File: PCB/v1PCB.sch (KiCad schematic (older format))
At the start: 223 parts, among them SW1 SW_PUSH, SW2 SW_PUSH, U1 STM32F072CBUx, U2 MCP1700-3302E_SOT23

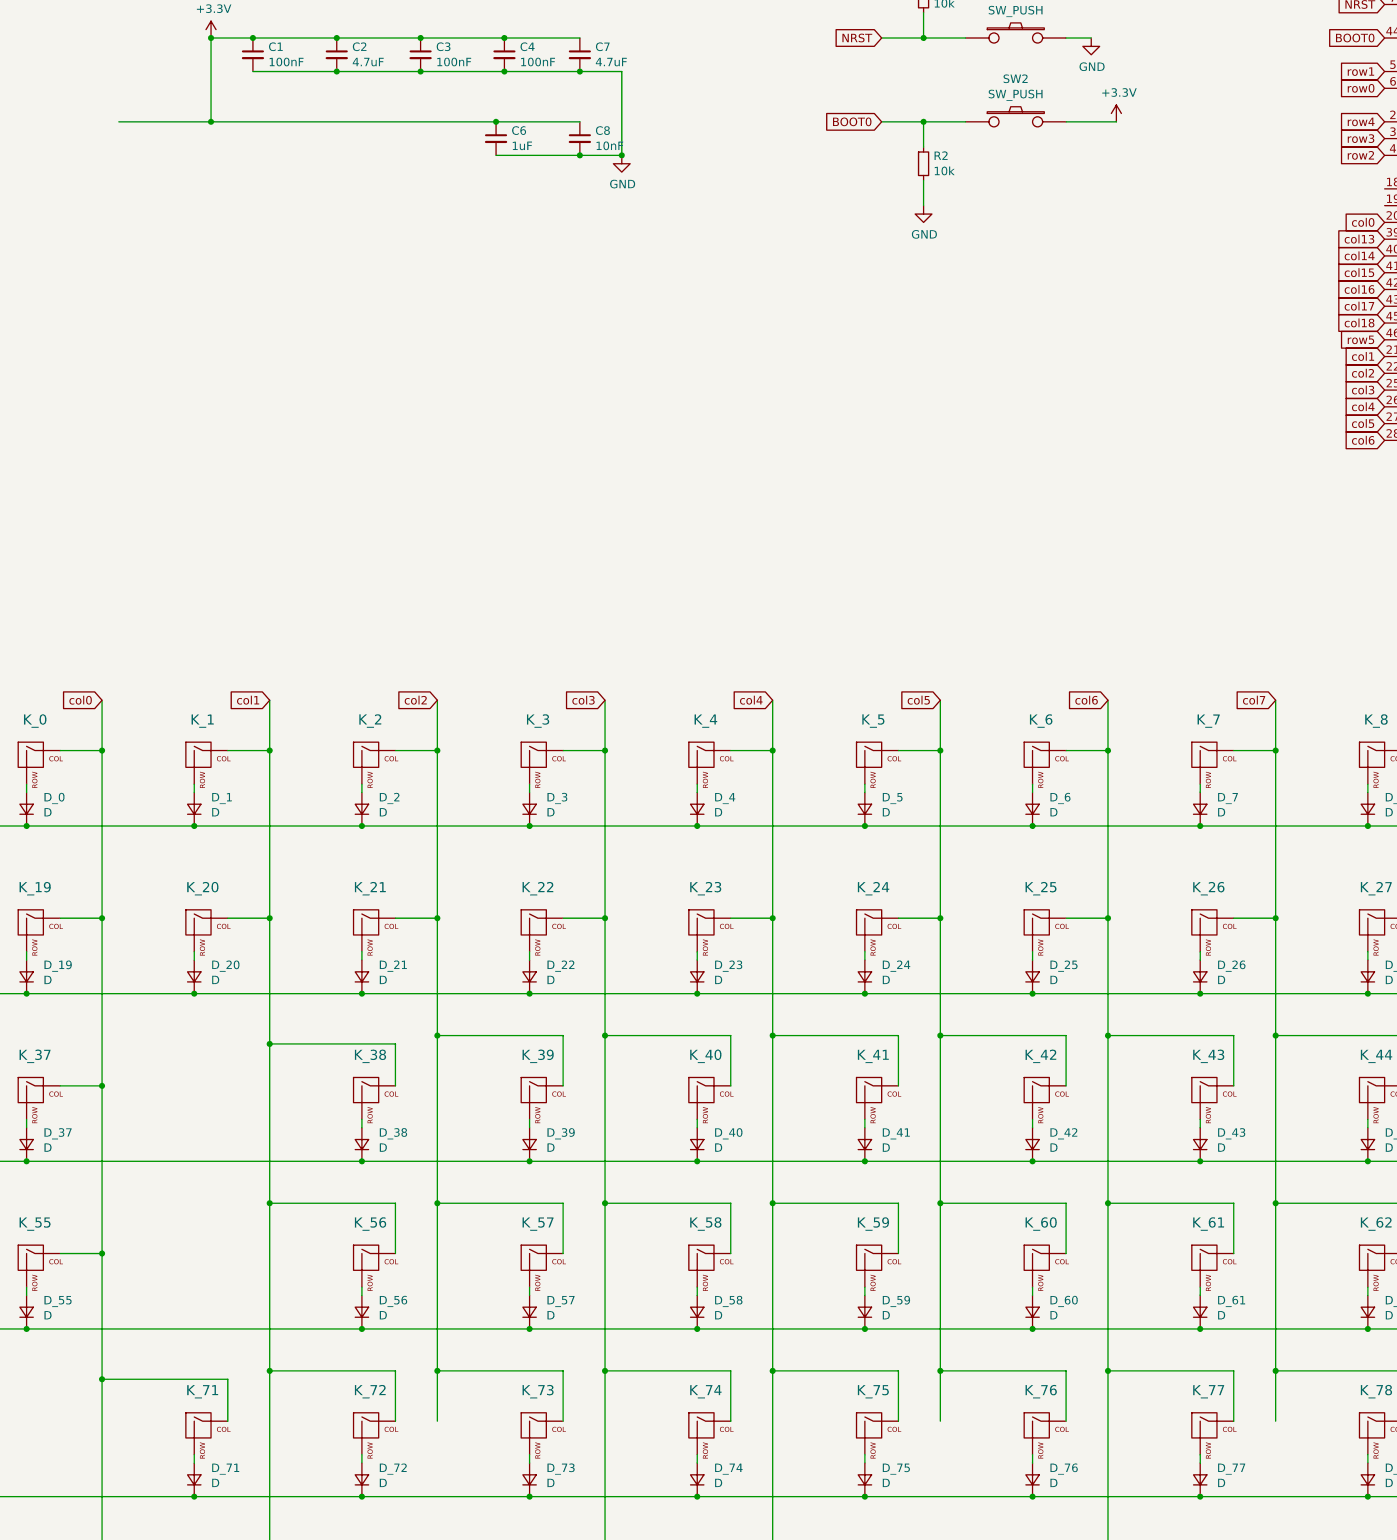
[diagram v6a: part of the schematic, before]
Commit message: PCB is being produced, because fuck it. CAD is being quoted.
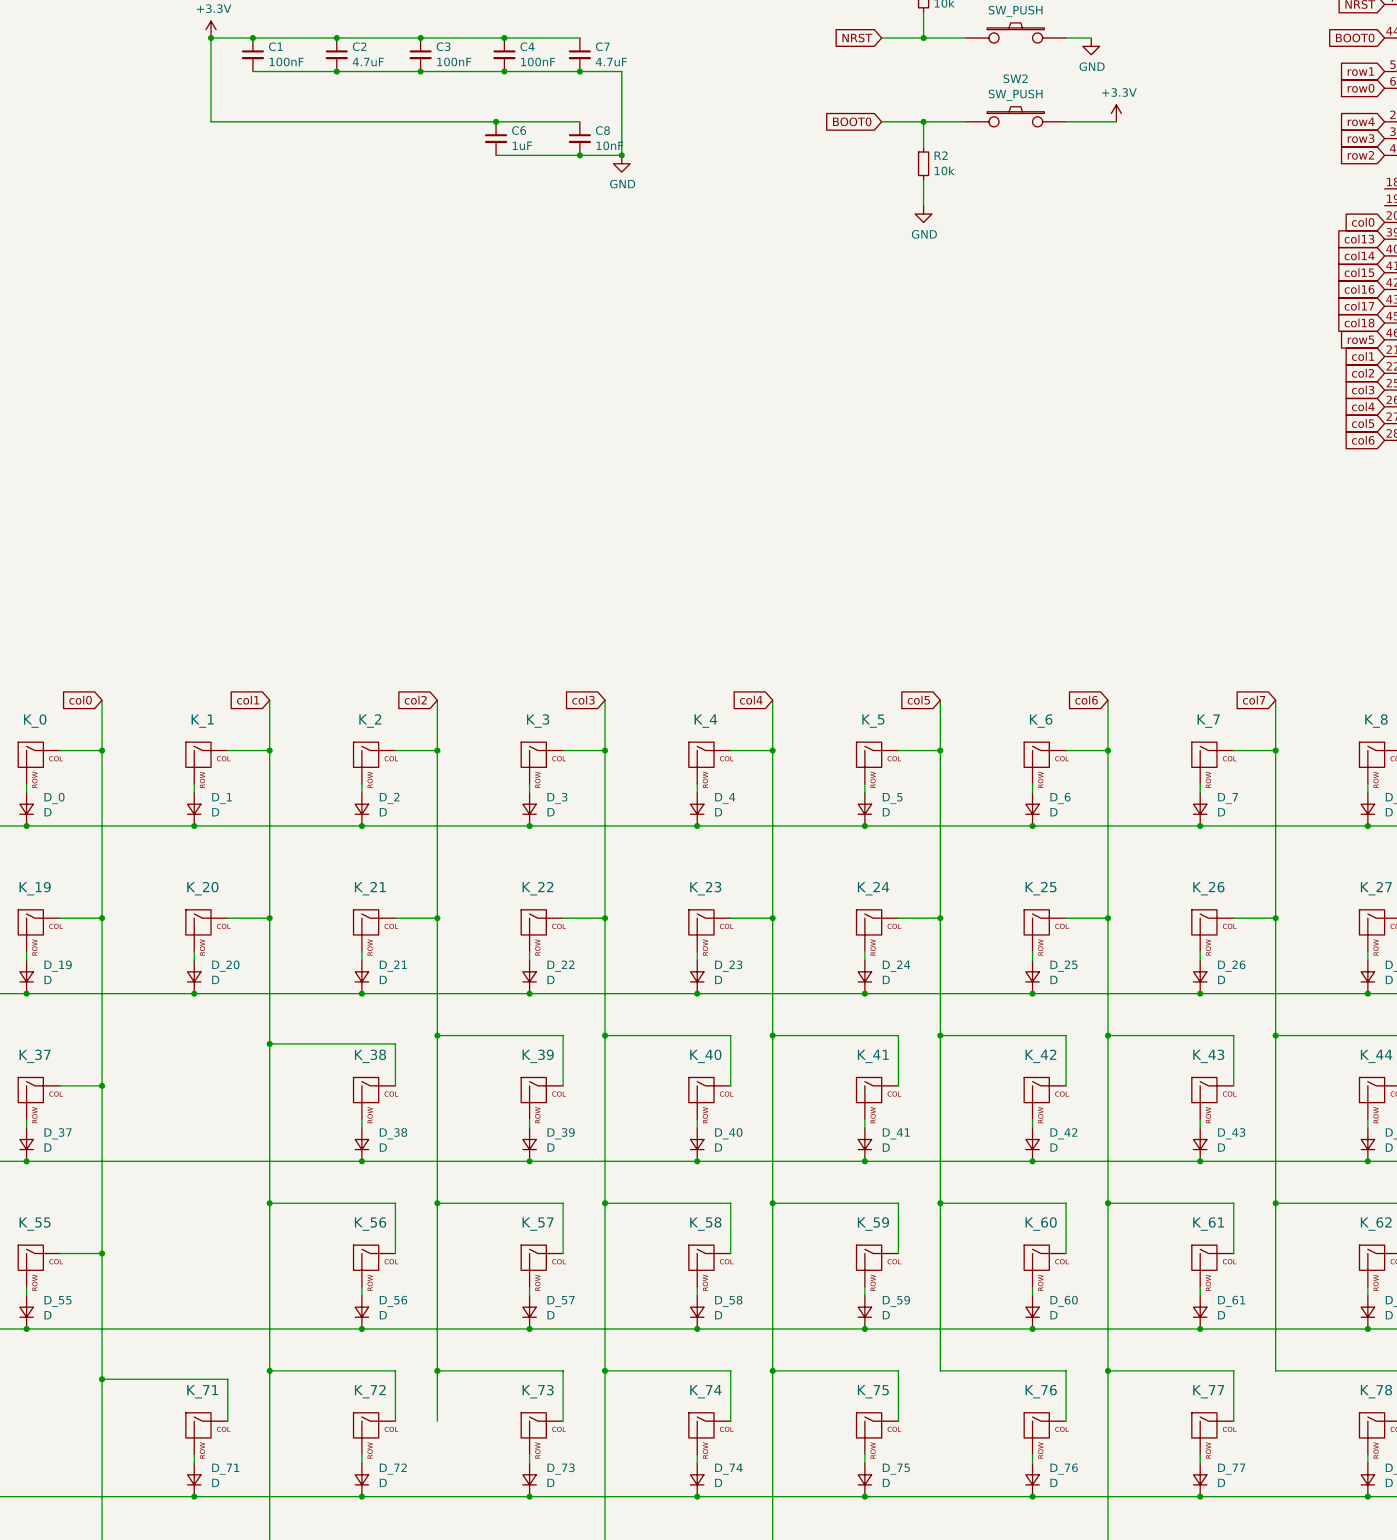
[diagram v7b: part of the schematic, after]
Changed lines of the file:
@@
 Wire Wire Line
 	3500 1500 3500 2000
-Wire Wire Line
-	2950 2000 3500 2000
 Connection ~ 3500 1500
 $Comp
@@
 	1    0    0    -1
 $EndComp
-Connection ~ 3500 2000
 Wire Wire Line
 	3500 2000 5200 2000
@@
 Wire Wire Line
 	8600 9450 7850 9450
-Connection ~ 7850 9450
-Wire Wire Line
-	7850 9450 7850 9750
 Wire Wire Line
 	9600 9750 9600 9450
@@
 Wire Wire Line
 	10600 9450 9850 9450
-Connection ~ 9850 9450
-Wire Wire Line
-	9850 9450 9850 9750
 Wire Wire Line
 	11600 9750 11600 9450

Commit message: Updates
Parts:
- K_93: footprint MX_Only:MXOnly-3U-NoLED -> MX_Only:MXOnly-2.75U-NoLED
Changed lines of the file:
@@
 F 0 "K_93" H 10450 11033 60  0000 C CNN
 F 1 "KEYSW" H 10450 10700 60  0001 C CNN
-F 2 "MX_Only:MXOnly-3U-NoLED" H 10450 10800 60  0001 C CNN
+F 2 "MX_Only:MXOnly-2.75U-NoLED" H 10450 10800 60  0001 C CNN
 F 3 "" H 10450 10800 60  0000 C CNN
 	1    10450 10800
